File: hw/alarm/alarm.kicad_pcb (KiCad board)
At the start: 2 copper layers, 3 parts, among them U1 RaspberryPi_Pico, U2 PEC11R-4215F-S0024

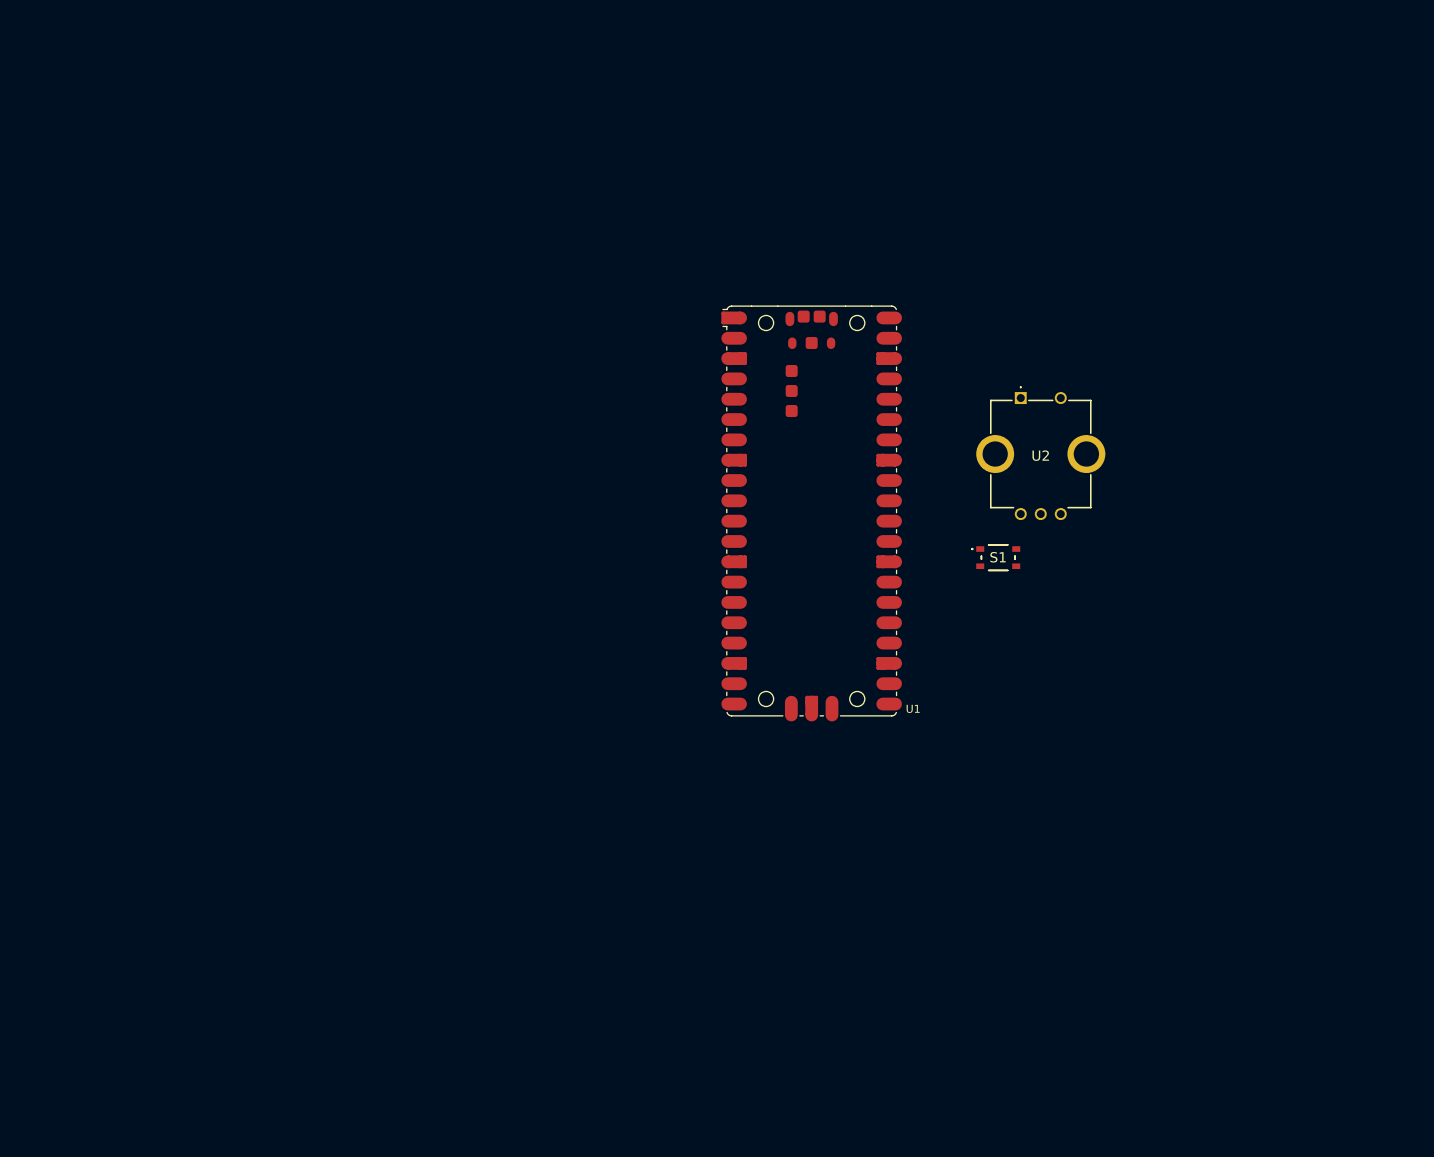
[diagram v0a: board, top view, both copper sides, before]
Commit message: Reorganize libraries, various updates to schematic
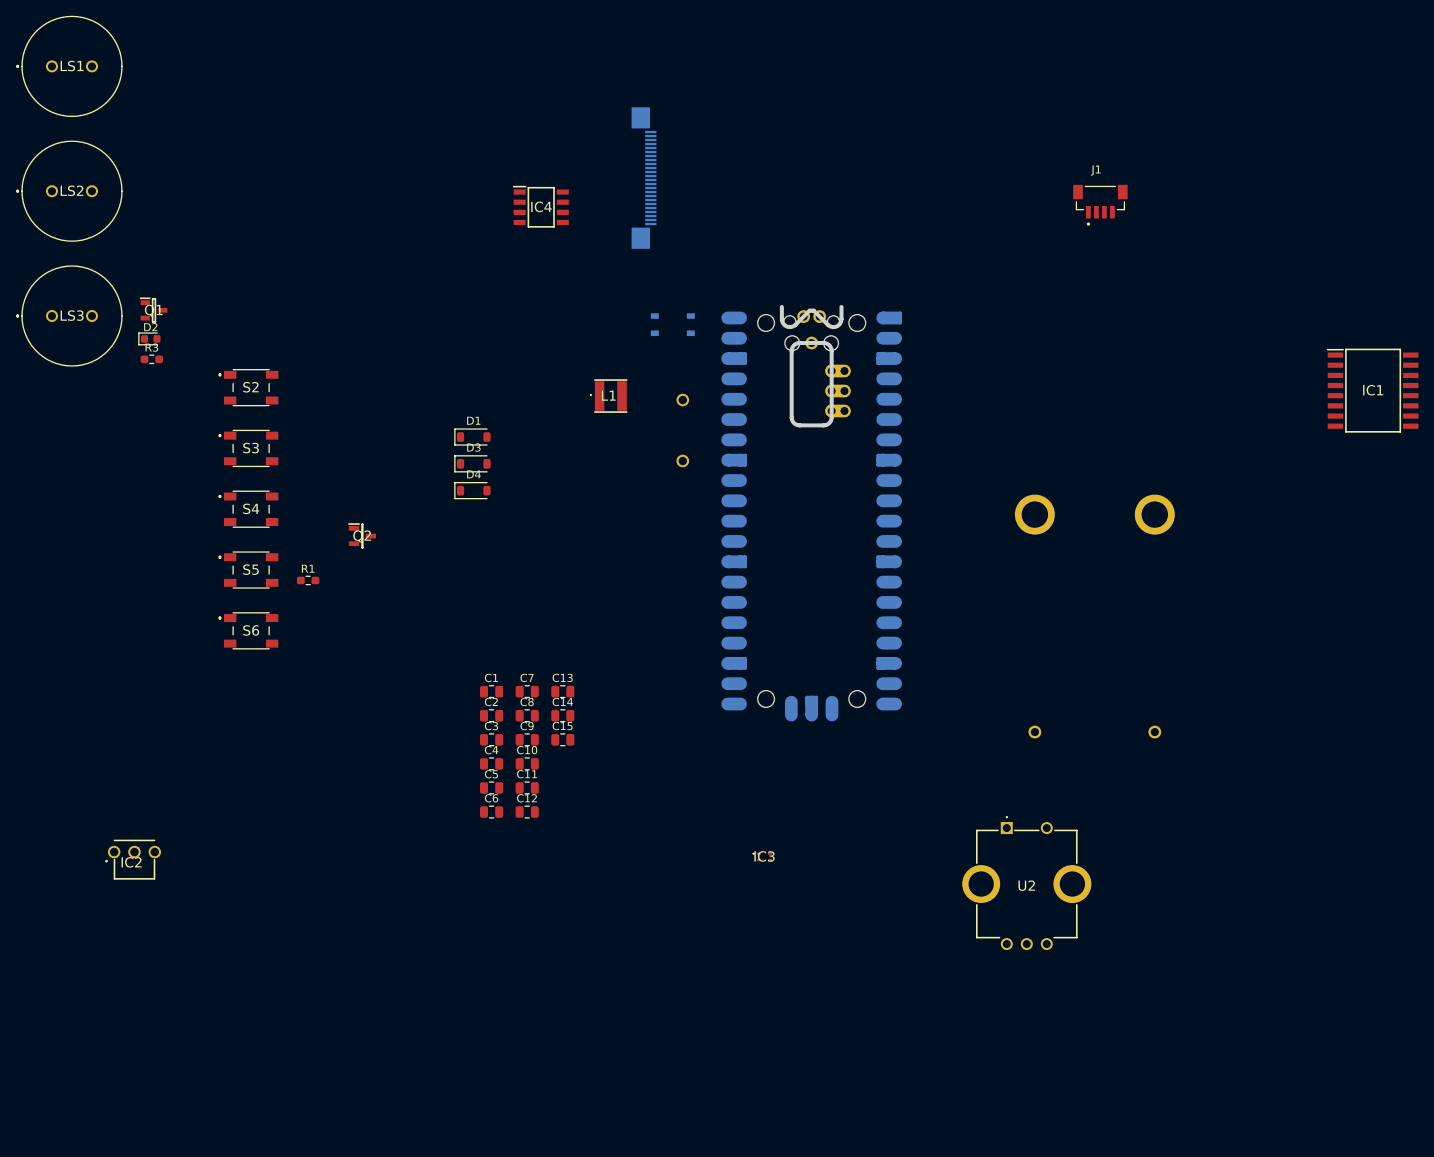
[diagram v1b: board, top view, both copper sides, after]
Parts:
- added C1: 1uF, Capacitor_SMD:C_0805_2012Metric, F.Cu at (99.6, 126.0)
- added C10: 10uF, Capacitor_SMD:C_0805_2012Metric, F.Cu at (104.0, 135.0)
- added C11: 1uF, Capacitor_SMD:C_0805_2012Metric, F.Cu at (104.0, 138.0)
- added C12: 10uF, Capacitor_SMD:C_0805_2012Metric, F.Cu at (104.0, 141.0)
- added C13: 1uF, Capacitor_SMD:C_0805_2012Metric, F.Cu at (108.5, 126.0)
- added C14: 0.1uF, Capacitor_SMD:C_0805_2012Metric, F.Cu at (108.5, 129.0)
- added C15: 0.1uF, Capacitor_SMD:C_0805_2012Metric, F.Cu at (108.5, 132.0)
- added C2: 0.1uF, Capacitor_SMD:C_0805_2012Metric, F.Cu at (99.6, 129.0)
- added C3: 1uF, Capacitor_SMD:C_0805_2012Metric, F.Cu at (99.6, 132.0)
- added C4: 1uF, Capacitor_SMD:C_0805_2012Metric, F.Cu at (99.6, 135.0)
- added C5: 1uF, Capacitor_SMD:C_0805_2012Metric, F.Cu at (99.6, 138.0)
- added C6: 1uF, Capacitor_SMD:C_0805_2012Metric, F.Cu at (99.6, 141.0)
- added C7: 1uF, Capacitor_SMD:C_0805_2012Metric, F.Cu at (104.0, 126.0)
- added C8: 1uF, Capacitor_SMD:C_0805_2012Metric, F.Cu at (104.0, 129.0)
- added C9: 1uF, Capacitor_SMD:C_0805_2012Metric, F.Cu at (104.0, 132.0)
- added D1: MBR0530, Diode_SMD:D_SOD-123, F.Cu at (97.4, 94.1)
- added D2: LED, LED_SMD:LED_0603_1608Metric, F.Cu at (57.0, 81.9)
- added D3: MBR0530, Diode_SMD:D_SOD-123, F.Cu at (97.4, 97.5)
- added D4: MBR0530, Diode_SMD:D_SOD-123, F.Cu at (97.4, 100.8)
- added IC1: DS3231S#T&R, SamacSys_Parts:SOIC127P1032X265-16N, F.Cu at (209.8, 88.3)
- added IC2: TSOP38238, SamacSys_Parts:TSOP38238, F.Cu at (55.0, 144.6)
- added IC3: SHT40-BD1B-R2, SamacSys_Parts:SHT40BD1BR2, F.Cu at (133.7, 146.6)
- added IC4: 23K256-I_SN, SamacSys_Parts:SOIC127P600X175-8N, F.Cu at (105.8, 65.4)
- added J1: 4328, 4328:ADAFRUIT_4328, F.Cu at (175.7, 64.2)
- added J2: SFV24R-4STBE1HLF, SamacSys_Parts:SFV24R4STBE1HLF, B.Cu at (117.2, 61.8)
- added L1: 10uH, SamacSys_Parts:NR4018T100M, F.Cu at (114.5, 89.0)
- added LS1: PT-1241PFQ, SamacSys_Parts:PT1241PFQ, F.Cu at (44.6, 47.8)
- added LS2: PT-1241PFQ, SamacSys_Parts:PT1241PFQ, F.Cu at (44.6, 63.4)
- added LS3: PT-1241PFQ, SamacSys_Parts:PT1241PFQ, F.Cu at (44.6, 79.0)
- added Q1: DMG2305UX-7, SamacSys_Parts:SOT96P240X115-3N, F.Cu at (57.4, 78.3)
- added Q2: IRLML2060TRPBF, SamacSys_Parts:SOT95P237X112-3N, F.Cu at (83.5, 106.5)
- added R1: 0.47Ω, Resistor_SMD:R_0603_1608Metric_Pad0.98x0.95mm_HandSolder, F.Cu at (76.7, 112.1)
- added R3: 267Ω, Resistor_SMD:R_0603_1608Metric_Pad0.98x0.95mm_HandSolder, F.Cu at (57.1, 84.4)
- added S2: PTS647SM70SMTR2LFS, SamacSys_Parts:PTS647SM38SMTR2LFS, F.Cu at (69.5, 88.0)
- added S3: PTS647SM70SMTR2LFS, SamacSys_Parts:PTS647SM38SMTR2LFS, F.Cu at (69.5, 95.5)
- added S4: PTS647SM70SMTR2LFS, SamacSys_Parts:PTS647SM38SMTR2LFS, F.Cu at (69.5, 103.2)
- added S5: PTS647SM70SMTR2LFS, SamacSys_Parts:PTS647SM38SMTR2LFS, F.Cu at (69.5, 110.8)
- added S6: PTS647SM70SMTR2LFS, SamacSys_Parts:PTS647SM38SMTR2LFS, F.Cu at (69.5, 118.3)
- added S7: DS01-254-L-01BE, SamacSys_Parts:DS01254L01BE, B.Cu at (123.5, 97.1)
- added U3: 2462, SamacSys_Parts:2462, B.Cu at (182.5, 131.0)
- S1: moved to B.Cu
- U1: footprint Module_RaspberryPi_Pico:RaspberryPi_Pico_Original_SMD -> Module_RaspberryPi_Pico:RaspberryPi_Pico_Original_SMD_MountingHoles_HandSolder_Castellated; moved to B.Cu
- moved U2 53.8 mm to (164.0, 143.0)
- moved S1 50.0 mm to (122.2, 80.1), turned to 180 degrees
- turned U1 to 180 degrees
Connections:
- U1 pad 1: unconnected-(U1-GPIO0-Pad1) -> /MOSI
- U1 pad 10: unconnected-(U1-GPIO7-Pad10) -> /EinkCS
- U1 pad 11: unconnected-(U1-GPIO8-Pad11) -> /Enc_A1
- U1 pad 12: unconnected-(U1-GPIO9-Pad12) -> /Enc_B1
- U1 pad 14: unconnected-(U1-GPIO10-Pad14) -> Net-(U1-GPIO10)
- U1 pad 15: unconnected-(U1-GPIO11-Pad15) -> Net-(U1-GPIO11)
- U1 pad 16: unconnected-(U1-GPIO12-Pad16) -> Net-(U1-GPIO12)
- U1 pad 17: unconnected-(U1-GPIO13-Pad17) -> Net-(U1-GPIO13)
- U1 pad 19: unconnected-(U1-GPIO14-Pad19) -> Net-(U1-GPIO14)
- U1 pad 2: unconnected-(U1-GPIO1-Pad2) -> /MISO
- U1 pad 20: unconnected-(U1-GPIO15-Pad20) -> Net-(U1-GPIO15)
- U1 pad 21: unconnected-(U1-GPIO16-Pad21) -> Net-(LS3-+)
- U1 pad 22: unconnected-(U1-GPIO17-Pad22) -> Net-(LS2-+)
- U1 pad 24: unconnected-(U1-GPIO18-Pad24) -> Net-(LS1-+)
- U1 pad 25: unconnected-(U1-GPIO19-Pad25) -> Net-(S7-NO)
- U1 pad 26: unconnected-(U1-GPIO20-Pad26) -> /EinkRESET
- U1 pad 27: unconnected-(U1-GPIO21-Pad27) -> /EinkBUSY
- U1 pad 29: unconnected-(U1-GPIO22-Pad29) -> Net-(IC2-OUT)
- U1 pad 36: unconnected-(U1-3V3-Pad36) -> +3.3V
- U1 pad 39: unconnected-(U1-VSYS-Pad39) -> Net-(Q1-S)
- U1 pad 4: unconnected-(U1-GPIO2-Pad4) -> /SCK
- U1 pad 40: unconnected-(U1-VBUS-Pad40) -> Net-(Q1-G)
- U1 pad 5: unconnected-(U1-GPIO3-Pad5) -> /DC
- U1 pad 6: unconnected-(U1-GPIO4-Pad6) -> /SDA
- U1 pad 7: unconnected-(U1-GPIO5-Pad7) -> /SCL
- U1 pad 9: unconnected-(U1-GPIO6-Pad9) -> /SRAMCS
- U1 pad D1: (no net) -> unconnected-(U1-SWCLK-PadD1)
- U1 pad D2: (no net) -> GND
- U1 pad D3: (no net) -> unconnected-(U1-SWDIO-PadD3)
- U2 pad 1: unconnected-(U2-COM-Pad1) -> GND
- U2 pad 2: unconnected-(U2-NO-Pad2) -> Net-(U1-GPIO10)
- U2 pad A1: unconnected-(U2-PadA1) -> /Enc_A1
- U2 pad B1: unconnected-(U2-PadB1) -> /Enc_B1
- U2 pad C1: unconnected-(U2-PadC1) -> GND
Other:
- board outline added: 7.5 x 14.8 mm

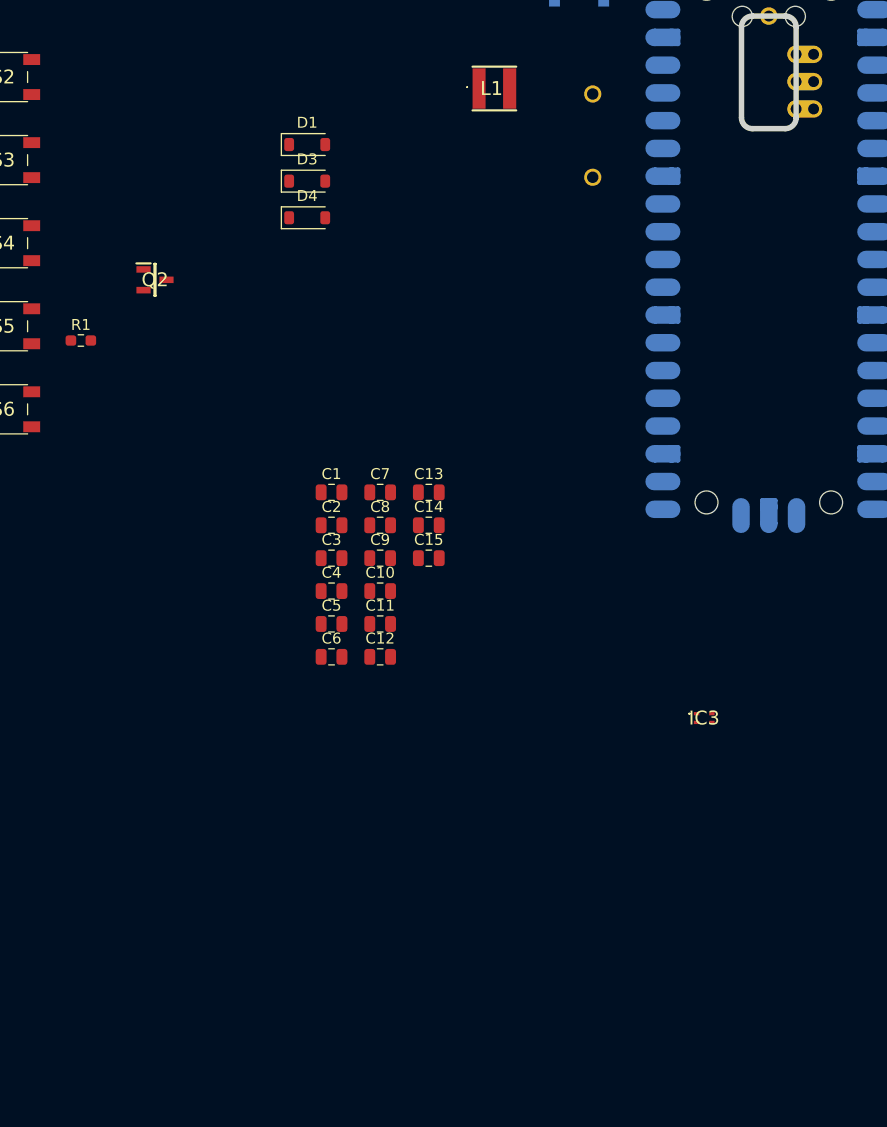
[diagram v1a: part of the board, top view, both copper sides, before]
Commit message: Add segment display circuit
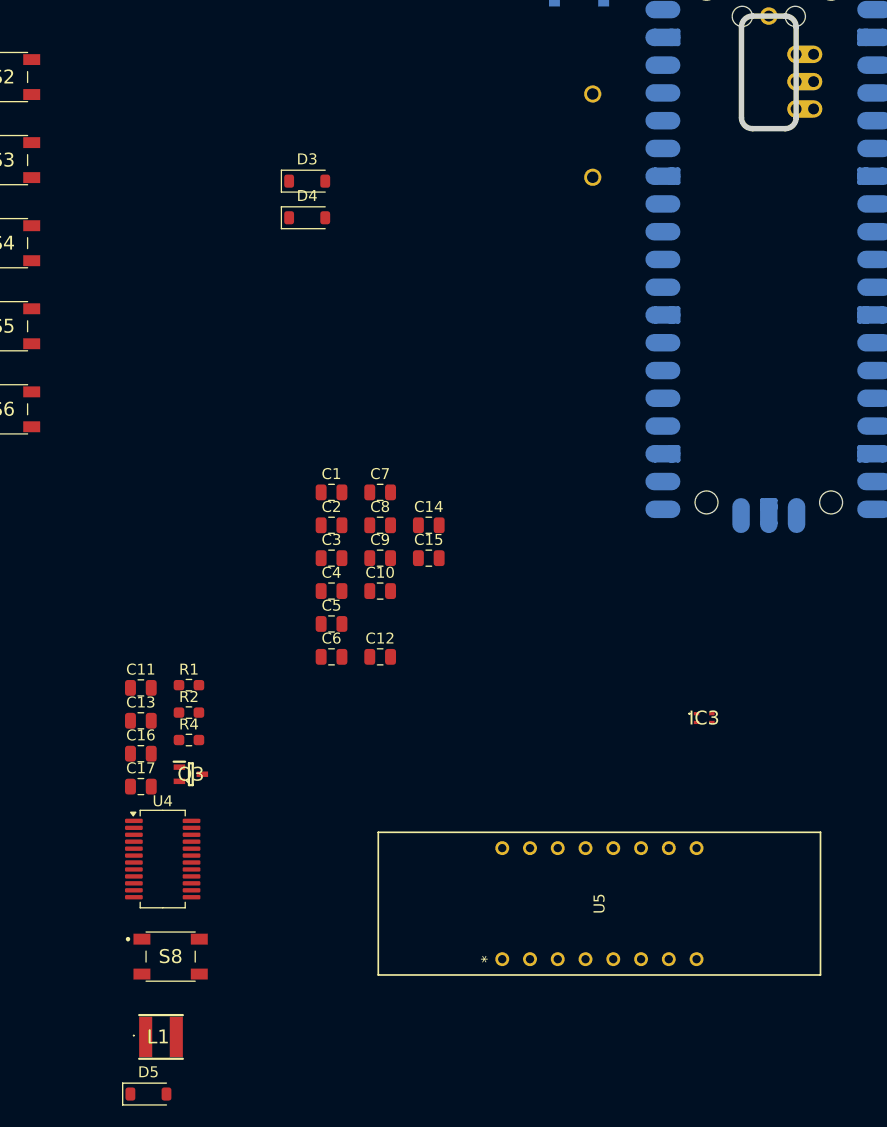
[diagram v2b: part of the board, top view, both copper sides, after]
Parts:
- removed D1: MBR0530, Diode_SMD:D_SOD-123
- removed Q2: IRLML2060TRPBF, SamacSys_Parts:SOT95P237X112-3N
- added C16: 4.7uF, Capacitor_SMD:C_0805_2012Metric, F.Cu at (82.2, 149.9)
- added C17: 0.1uF, Capacitor_SMD:C_0805_2012Metric, F.Cu at (82.2, 152.9)
- added D5: MBR0530, Diode_SMD:D_SOD-123, F.Cu at (82.8, 181.0)
- added Q3: Si1308EDL-T1-GE3, SamacSys_Parts:SOT65P210X110-3N, F.Cu at (86.7, 151.7)
- added R2: 10kΩ, Resistor_SMD:R_0603_1608Metric_Pad0.98x0.95mm_HandSolder, F.Cu at (86.6, 146.1)
- added R4: 10kΩ, Resistor_SMD:R_0603_1608Metric_Pad0.98x0.95mm_HandSolder, F.Cu at (86.6, 148.6)
- added S8: PTS647SM70SMTR2LFS, SamacSys_Parts:PTS647SM38SMTR2LFS, F.Cu at (84.9, 168.4)
- added U4: AS1115-BSST, Package_SO:QSOP-24_3.9x8.7mm_P0.635mm, F.Cu at (84.2, 159.5)
- added U5: TDCR1060M, footprints:TDCG1060M_VIS, F.Cu at (115.2, 168.7)
- C1, C11, C13, C3, C4, C5, C6, C7, C8, C9: value 1uF -> 0.1uF
- C10, C12: value 10uF -> 4.7uF
- moved L1 92.0 mm to (84.0, 175.8)
- moved C13 33.6 mm to (82.2, 146.8)
- moved R1 33.0 mm to (86.6, 143.6)
- moved C11 22.7 mm to (82.2, 143.8)
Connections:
- C11 pad 1: /VGL -> GND
- C11 pad 2: GND -> /VGL
- C13 pad 1: /VGH -> GND
- C13 pad 2: GND -> /VGH
- R1 pad 1: GND -> /RESE
- R1 pad 2: /RESE -> GND
- S2 pad 2: Net-(U1-GPIO12) -> Net-(U4-SEGD)
- S2 pad 3: GND -> /KEYA
- S3 pad 2: Net-(U1-GPIO13) -> Net-(U4-SEGC)
- S3 pad 3: GND -> /KEYA
- S4 pad 2: Net-(U1-GPIO14) -> Net-(U4-SEGB)
- S4 pad 3: GND -> /KEYA
- S5 pad 2: Net-(U1-GPIO15) -> Net-(U4-SEGA)
- S5 pad 3: GND -> /KEYA
- S6 pad 2: Net-(U1-GPIO11) -> Net-(U4-SEGE)
- S6 pad 3: GND -> /KEYA
- U1 pad 15: Net-(U1-GPIO11) -> /IRQ
- U1 pad 16: Net-(U1-GPIO12) -> /ANODE_L3
- U1 pad 17: Net-(U1-GPIO13) -> /ANODE_L1_L2
- U1 pad 19: Net-(U1-GPIO14) -> unconnected-(U1-GPIO14-Pad19)
- U1 pad 20: Net-(U1-GPIO15) -> unconnected-(U1-GPIO15-Pad20)

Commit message: Start board layout
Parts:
- removed U3: 2462, SamacSys_Parts:2462
- added BT1: 2464, SamacSys_Parts:2464, B.Cu at (99.6, 71.6)
- C1, C11, C13, C14, C15, C17, C2, C3, C4, C5, C6, C7, C8, C9: value 0.1uF -> 1uF
- J1, Q1: moved to B.Cu
- J2: moved to F.Cu
- L1: value 10uH -> 68 uH; footprint SamacSys_Parts:NR4018T100M -> SamacSys_Parts:INDM3225X240N
- moved D2 137.6 mm to (187.0, 127.0)
- moved IC2 132.6 mm to (185.2, 119.7)
- moved R3 132.4 mm to (182.5, 127.0)
- moved IC1 114.1 mm to (100.5, 121.0)
- moved S6 99.3 mm to (159.9, 159.5), turned to 90 degrees
- moved D5 96.5 mm to (104.5, 87.0)
- moved S5 96.0 mm to (152.3, 159.5), turned to 90 degrees
- moved S4 93.9 mm to (144.7, 159.5), turned to 90 degrees
- moved S2 93.3 mm to (129.5, 159.5), turned to 90 degrees
- moved S3 93.0 mm to (137.1, 159.5), turned to 90 degrees
- moved Q1 91.9 mm to (148.9, 70.0), turned to 180 degrees
- moved IC3 89.9 mm to (104.3, 61.6)
- moved L1 87.7 mm to (104.5, 90.5)
- moved S8 83.1 mm to (167.5, 159.5), turned to 90 degrees
- moved C14 82.7 mm to (191.1, 124.5)
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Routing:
- net Net-(U4-SEGDP): track 0.00 -> 51.4 mm
- net +3.3V: track 0.00 -> 44.6 mm
- net Net-(U4-DIG4): track 0.00 -> 38.5 mm
- net Net-(U4-SEGD): track 0.00 -> 36.4 mm
- net Net-(U4-DIG5): track 0.00 -> 36.0 mm
- net Net-(U4-DIG3): track 0.00 -> 35.2 mm
- net Net-(U4-SEGF): track 0.00 -> 33.3 mm
- net Net-(U4-SEGC): track 0.00 -> 31.0 mm
- net Net-(U4-DIG2): track 0.00 -> 30.9 mm
- net Net-(U4-DIG1): track 0.00 -> 26.6 mm
- net Net-(U4-SEGG): track 0.00 -> 24.3 mm
- net Net-(U4-DIG0): track 0.00 -> 24.1 mm
- net Net-(U4-SEGB): track 0.00 -> 20.5 mm
- net /RESE: track 0.00 -> 11.5 mm
- net Net-(S7-NO): track 0.00 -> 10.9 mm
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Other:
- board size 7.5 x 14.8 mm -> 106 x 64.5 mm

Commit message: Continue board layout
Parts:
- removed BT1: 2464, SamacSys_Parts:2464
- removed U2: PEC11R-4215F-S0024, SamacSys_Parts:PEC11R4215FS0024
- added IC5: PEC11S-929K-S0015, SamacSys_Parts:PEC11S929KS0015, F.Cu at (180.6, 108.0)
- added REF**: MountingHole_2.2mm_M2_DIN965_Pad, MountingHole:MountingHole_2.2mm_M2_DIN965_Pad, F.Cu at (190.5, 131.5)
- added REF**: MountingHole_2.2mm_M2_DIN965_Pad, MountingHole:MountingHole_2.2mm_M2_DIN965_Pad, F.Cu at (91.5, 64.5)
- added REF**: MountingHole_2.2mm_M2_DIN965_Pad, MountingHole:MountingHole_2.2mm_M2_DIN965_Pad, F.Cu at (190.5, 64.5)
- added REF**: MountingHole_2.2mm_M2_DIN965_Pad, MountingHole:MountingHole_2.2mm_M2_DIN965_Pad, F.Cu at (91.5, 131.5)
- added U3: 2462, SamacSys_Parts:2462, B.Cu at (99.5, 71.0)
- LS1, LS2, LS3: moved to B.Cu
- moved LS1 110.5 mm to (164.5, 99.5), turned to 180 degrees
- moved LS2 95.1 mm to (149.5, 99.5), turned to 180 degrees
- moved LS3 84.4 mm to (134.5, 99.5), turned to 180 degrees
- moved C15 63.2 mm to (102.9, 124.5)
- moved IC3 63.2 mm to (98.7, 124.6)
- moved J1 54.3 mm to (131.7, 81.0), turned to -90 degrees
- moved C1 53.9 mm to (107.0, 104.0)
- moved IC4 53.9 mm to (100.5, 105.5)
- moved S7 52.4 mm to (128.6, 65.5), turned to 90 degrees
- moved S2 36.5 mm to (131.1, 123.0)
- moved S3 36.5 mm to (138.7, 123.0)
- moved S4 36.5 mm to (146.3, 123.0)
- moved S5 36.5 mm to (153.9, 123.0)
- moved S6 36.5 mm to (161.5, 123.0)
- moved S8 36.5 mm to (169.1, 123.0)
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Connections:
- S8 pad 1: /KEYA -> unconnected-(S8-Pad1)
- S8 pad 3: unconnected-(S8-Pad3) -> /KEYA
- U1 pad 14: Net-(U1-GPIO10) -> /Enc_Switch
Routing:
- net /KEYA: track 0.00 -> 53.6 mm
- net +3.3V: track 44.6 -> 18.8 mm
- net Net-(D3-A): track 0.00 -> 15.9 mm
- net Net-(J2-VSL): track 0.00 -> 14.8 mm
- net Net-(S7-NO): track 10.9 -> 0.00 mm
- net Net-(S1-COM_2): track 10.6 -> 0.00 mm
- net Net-(Q1-S): track 9.96 -> 0.00 mm
- net Net-(D5-A): track 7.58 -> 17.2 mm
- net Net-(Q1-G): track 9.18 -> 0.00 mm
- net Net-(J2-VCOM): track 5.94 -> 12.3 mm
- net GND: track 0.00 -> 3.69 mm
- net Net-(IC2-OUT): track 0.00 -> 3.27 mm
- net Net-(D2-A): track 0.00 -> 1.80 mm
- net /SCL: track 7.60 -> 6.18 mm
- net /SDA: track 7.71 -> 8.66 mm
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- added copper zone on B.Cu, net GND
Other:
- board size 106 x 64.5 mm -> 105 x 73 mm
